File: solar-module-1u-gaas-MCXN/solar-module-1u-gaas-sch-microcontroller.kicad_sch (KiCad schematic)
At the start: 43 parts, among them U1 MCXN947VKLT, U11 TCAN330, U2 TMP101NA/3KSLOTTED, U7 TMP101NA/3KSLOTTED, Y2 24 MHz

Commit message: Now solar module v1.2.
Upgraded CAN transciever to the 337, added version bits, removed silkscreen on cell outlines, double checked fastener heads, cleaned up documentation a lot, fixed ERCs and DRCs.
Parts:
- C1, C11, C26, C28, C3, C46, C48, C49, C5, C50, C51, C52, C53: DPN 587-3472-1-ND -> 399-6856-1-ND; MFR Taiyo Yuden -> KEMET; MPN TMK107BJ104KAHT -> C0603C104K5RACAUTO
- C16, C25: DPN 490-GRM1885C1H4R7WA01DCT-ND -> 399-15924-1-ND; MFR Murata -> KEMET; MPN GRM1885C1H4R7WA01D -> C0603C479D5GACAUTO
- C27, C30: DPN 587-4332-1-ND -> 490-GRT188C71C475KE13DCT-ND; MFR Taiyo Yuden -> Murata Electronics; MPN EMK107BBJ475KAHT -> GRT188C71C475KE13D
- C29: footprint oresat-passives:0805-C-NOSILK -> oresat-passives:1206-C; DPN 490-9959-1-ND -> 490-12409-1-ND; MPN GRM21BR61E226ME44L -> GRT31CC81C226KE01L
- C31: DPN 587-4929-1-ND -> 490-GRT188C71E225KE13DCT-ND; MFR Taiyo Yuden -> Murata Electronics; MPN TMK107BBJ225MAHT -> GRT188C71E225KE13D
- C47: DPN 587-3473-1-ND -> 490-GRT188R71E105KE13DCT-ND; MFR Taiyo Yuden -> Murata Electronics; MPN TMK107BJ105KAHT -> GRT188R71E105KE13D
- D4: value AMBER -> AMB; now not fitted
- D7: value AMBER -> AMB
- U11: value TCAN330 -> TCAN337G; symbol Interface_CAN_LIN:TCAN330 -> Interface_CAN_LIN:TCAN337G; DPN 296-46215-1-ND -> TCAN337GD-ND; MPN TCAN330DCNR -> TCAN337GD
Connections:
- net GND: now also U1.89 (P0_21), U1.90 (P0_22), U1.91 (P0_23)
- net CAN-FAULT: now reaches U11.5 (FAULT)
- net CAN-FAULT: now also U1.5 (P1_12)
- net CAN-SILENT: now reaches U11.8 (S)
- net CAN-SILENT: now also U1.7 (P1_14)
- net MCU-LED: now reaches R21.1, R5.1, U1.6 (P1_13)
- no-connect marks 64 -> 57
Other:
- note added: "(hand placed)"
- note added: "1206"
- note added: "Hardware version number (use pullups)"
- note added: "Rev: 000"
- moved on the sheet: C1, C16, C25, C28, C3, D7, R21, R23, R24, R3, R4, R5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

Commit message: Fixed Makefile to produce usable BOM. Updated BOM to correct DPNs, updated EOL'd components
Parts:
- FB1, L3, R23, R24, Y2: DIS DIgiKey -> DigiKey
- R21, R5: DPN RMCF0603FT2K00TR-ND -> RMCF0603FT2K00CT-ND
- U2, U7: DIS DIgiKey -> DigiKey; DPN 296-27725-2-ND -> 296-27725-1-ND
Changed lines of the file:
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@@
 			)
 		)
-		(property "DPN" "RMCF0603FT2K00TR-ND"
+		(property "DPN" "RMCF0603FT2K00CT-ND"
 			(at 124.46 69.85 0)
 			(hide yes)
@@
 			)
 		)
-		(property "DPN" "RMCF0603FT2K00TR-ND"
+		(property "DPN" "RMCF0603FT2K00CT-ND"
 			(at 139.7 69.85 0)
 			(hide yes)
@@
 			)
 		)
-		(property "DIS" "DIgiKey"
+		(property "DIS" "DigiKey"
 			(at 101.6 76.2 90)
 			(hide yes)
@@
 			)
 		)
-		(property "DIS" "DIgiKey"
+		(property "DIS" "DigiKey"
 			(at 403.86 97.79 0)
 			(hide yes)
@@
 			)
 		)
-		(property "DIS" "DIgiKey"
+		(property "DIS" "DigiKey"
 			(at 375.92 121.92 90)
 			(hide yes)
@@
 			)
 		)
-		(property "DIS" "DIgiKey"
+		(property "DIS" "DigiKey"
 			(at 154.94 190.5 0)
 			(hide yes)
@@
 			)
 		)
-		(property "DPN" "296-27725-2-ND"
+		(property "DPN" "296-27725-1-ND"
 			(at 154.94 190.5 0)
 			(hide yes)
@@
 			)
 		)
-		(property "DIS" "DIgiKey"
+		(property "DIS" "DigiKey"
 			(at 154.94 144.78 0)
 			(hide yes)
@@
 			)
 		)
-		(property "DPN" "296-27725-2-ND"
+		(property "DPN" "296-27725-1-ND"
 			(at 154.94 144.78 0)
 			(hide yes)
@@
 			)
 		)
-		(property "DIS" "DIgiKey"
+		(property "DIS" "DigiKey"
 			(at 223.52 134.62 0)
 			(hide yes)
@@
 			)
 		)
-		(property "DIS" "DIgiKey"
+		(property "DIS" "DigiKey"
 			(at 236.22 134.62 0)
 			(hide yes)

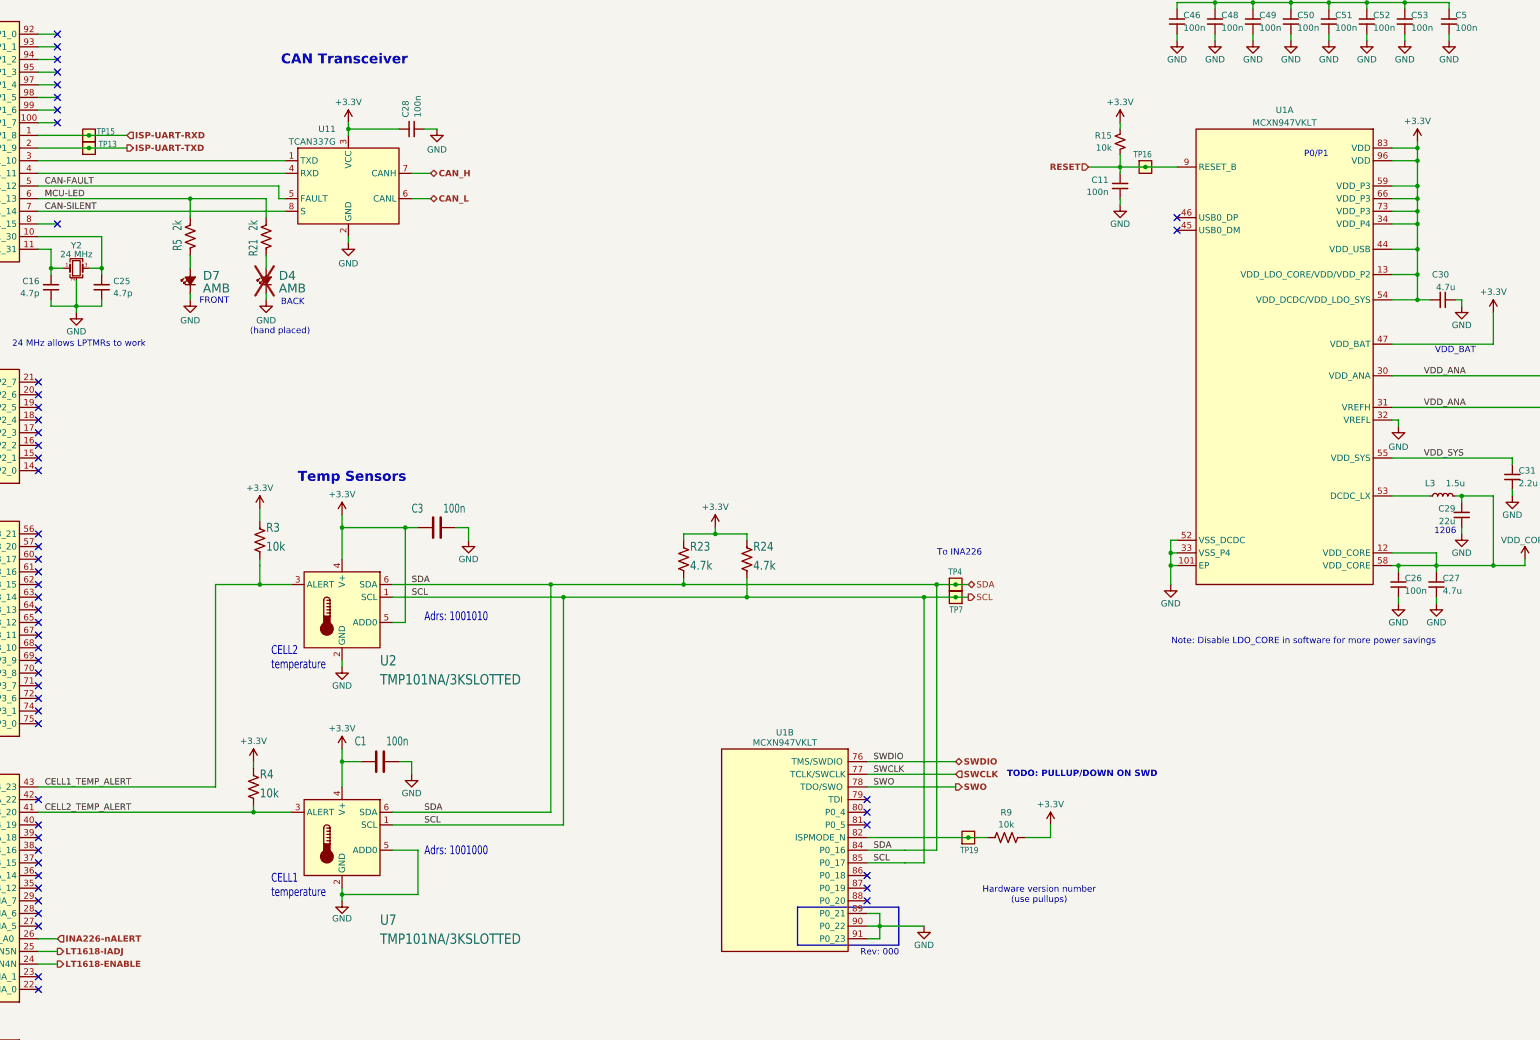
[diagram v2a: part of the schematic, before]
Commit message: Minor polishing to schematic and board: fixed value font sizes and placement, imported value fixes to layout.
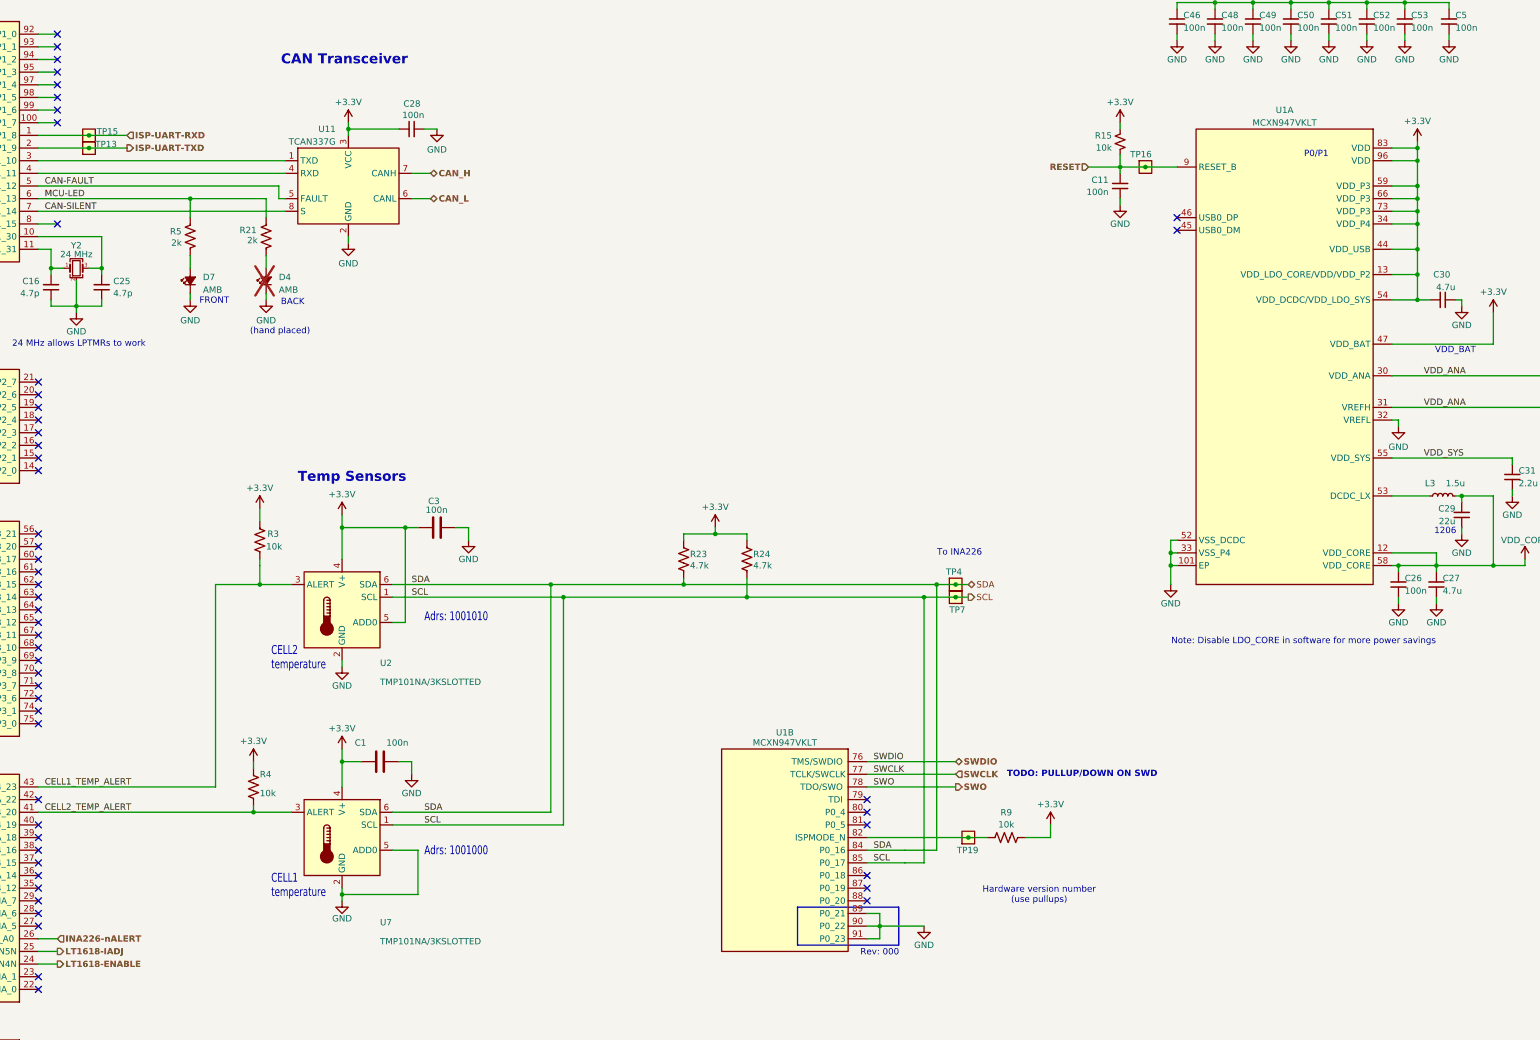
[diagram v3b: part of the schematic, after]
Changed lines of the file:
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@@
 		(dnp no)
 		(property "Reference" "C30"
-			(at 377.19 77.47 90)
+			(at 377.444 77.47 90)
 			(show_name no)
 			(do_not_autoplace no)
@@
 			(effects
 				(font
-					(size 1.778 1.778)
+					(size 1.27 1.27)
 				)
 				(justify right top)
@@
 			(effects
 				(font
-					(size 1.778 1.778)
+					(size 1.27 1.27)
 				)
 				(justify right top)
@@
 		(dnp no)
 		(property "Reference" "C3"
-			(at 168.91 125.476 90)
+			(at 172.212 123.698 90)
 			(show_name no)
 			(do_not_autoplace no)
 			(effects
 				(font
-					(size 1.778 1.27)
+					(size 1.27 1.27)
 				)
 				(justify right bottom)
@@
 		)
 		(property "Value" "100n"
-			(at 175.26 125.476 90)
+			(at 171.704 125.476 90)
 			(show_name no)
 			(do_not_autoplace no)
 			(effects
 				(font
-					(size 1.778 1.27)
+					(size 1.27 1.27)
 				)
 				(justify right bottom)
@@
 			(effects
 				(font
-					(size 1.27 1.0795)
+					(size 1.27 1.27)
 				)
 				(justify left)
@@
 		(dnp no)
 		(property "Reference" "R5"
-			(at 122.936 70.358 90)
+			(at 120.396 68.072 0)
 			(show_name no)
 			(do_not_autoplace no)
 			(effects
 				(font
-					(size 1.778 1.27)
+					(size 1.27 1.27)
 				)
 				(justify right top)
@@
 		)
 		(property "Value" "2k"
-			(at 122.936 66.548 90)
+			(at 120.65 70.358 0)
 			(show_name no)
 			(do_not_autoplace no)
 			(effects
 				(font
-					(size 1.778 1.27)
+					(size 1.27 1.27)
 				)
 				(justify right top)
@@
 			(effects
 				(font
-					(size 1.778 1.27)
+					(size 1.27 1.27)
 				)
 				(justify right bottom)
@@
 			(effects
 				(font
-					(size 1.778 1.27)
+					(size 1.27 1.27)
 				)
 				(justify right bottom)
@@
 			(effects
 				(font
-					(size 1.27 1.0795)
+					(size 1.27 1.27)
 				)
 				(justify left)
@@
 		(dnp no)
 		(property "Reference" "R21"
-			(at 138.176 70.358 90)
+			(at 134.366 67.818 0)
 			(show_name no)
 			(do_not_autoplace no)
 			(effects
 				(font
-					(size 1.778 1.27)
+					(size 1.27 1.27)
 				)
 				(justify right top)
@@
 		)
 		(property "Value" "2k"
-			(at 138.176 66.548 90)
+			(at 135.89 69.85 0)
 			(show_name no)
 			(do_not_autoplace no)
 			(effects
 				(font
-					(size 1.778 1.27)
+					(size 1.27 1.27)
 				)
 				(justify right top)
@@
 			(effects
 				(font
-					(size 1.778 1.5113)
+					(size 1.27 1.27)
 				)
 				(justify right)
@@
 			(effects
 				(font
-					(size 1.778 1.5113)
+					(size 1.27 1.27)
 				)
 				(justify right)
@@
 			(effects
 				(font
-					(size 1.778 1.778)
+					(size 1.27 1.27)
 				)
 				(justify right top)
@@
 			(effects
 				(font
-					(size 1.778 1.778)
+					(size 1.27 1.27)
 				)
 				(justify right top)
@@
 		(dnp no)
 		(property "Reference" "C28"
-			(at 167.7041 45.9359 0)
+			(at 170.688 43.18 90)
 			(show_name no)
 			(do_not_autoplace no)
@@
 		)
 		(property "Value" "100n"
-			(at 170.1284 45.9359 0)
+			(at 171.45 45.466 90)
 			(show_name no)
 			(do_not_autoplace no)
@@
 			(effects
 				(font
-					(size 1.27 1.0795)
+					(size 1.27 1.27)
 				)
 				(justify left)
@@
 			(effects
 				(font
-					(size 1.27 1.0795)
+					(size 1.27 1.27)
 				)
 				(justify left)
@@
 			(effects
 				(font
-					(size 1.27 1.0795)
+					(size 1.27 1.27)
 				)
 				(justify left)
@@
 			(effects
 				(font
-					(size 2.0828 1.7703)
+					(size 1.27 1.27)
 				)
 				(justify right bottom)
@@
 			(effects
 				(font
-					(size 2.0828 1.7703)
+					(size 1.27 1.27)
 				)
 				(justify right bottom)
@@
 		(dnp no)
 		(property "Reference" "R3"
-			(at 139.7 128.27 0)
+			(at 139.954 129.54 0)
 			(show_name no)
 			(do_not_autoplace no)
 			(effects
 				(font
-					(size 1.778 1.5113)
+					(size 1.27 1.27)
 				)
 				(justify right)
@@
 			(effects
 				(font
-					(size 1.778 1.5113)
+					(size 1.27 1.27)
 				)
 				(justify right)
@@
 			(effects
 				(font
-					(size 2.0828 1.7703)
+					(size 1.27 1.27)
 				)
 				(justify right bottom)
@@
 			(effects
 				(font
-					(size 2.0828 1.7703)
+					(size 1.27 1.27)
 				)
 				(justify right bottom)
@@
 		(dnp no)
 		(property "Reference" "R23"
-			(at 224.79 132.08 0)
+			(at 224.79 133.604 0)
 			(show_name no)
 			(do_not_autoplace no)
 			(effects
 				(font
-					(size 1.778 1.5113)
+					(size 1.27 1.27)
 				)
 				(justify right)
@@
 			(effects
 				(font
-					(size 1.778 1.5113)
+					(size 1.27 1.27)
 				)
 				(justify right)
@@
 		(dnp no)
 		(property "Reference" "R24"
-			(at 237.49 132.08 0)
+			(at 237.49 133.604 0)
 			(show_name no)
 			(do_not_autoplace no)
 			(effects
 				(font
-					(size 1.778 1.5113)
+					(size 1.27 1.27)
 				)
 				(justify right)
@@
 			(effects
 				(font
-					(size 1.778 1.5113)
+					(size 1.27 1.27)
 				)
 				(justify right)
@@
 			(effects
 				(font
-					(size 1.27 1.0795)
+					(size 1.27 1.27)
 				)
 				(justify left)
